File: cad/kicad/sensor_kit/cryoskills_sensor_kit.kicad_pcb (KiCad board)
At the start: 2 copper layers, 150 x 60 mm, 51 parts, among them J1 PWR_In, J10 QWIIC_I2C_2, J11 QWIIC_I2C_3, J12 DS18B20, J2 PWR_SENSE_Panel, J3 PWR_SENSE_Battery, J4 Conn_01x02, J5 Conn_01x02, J6 Conn_01x02, J7 PT1000_RTD, J8 SPI_BREAKOUT, J9 QWIIC_I2C_1, SW1 SPDT Switch, U1 LM317_TO-220, U2 RFM96W, U3 INA3221, U4 LM334Z

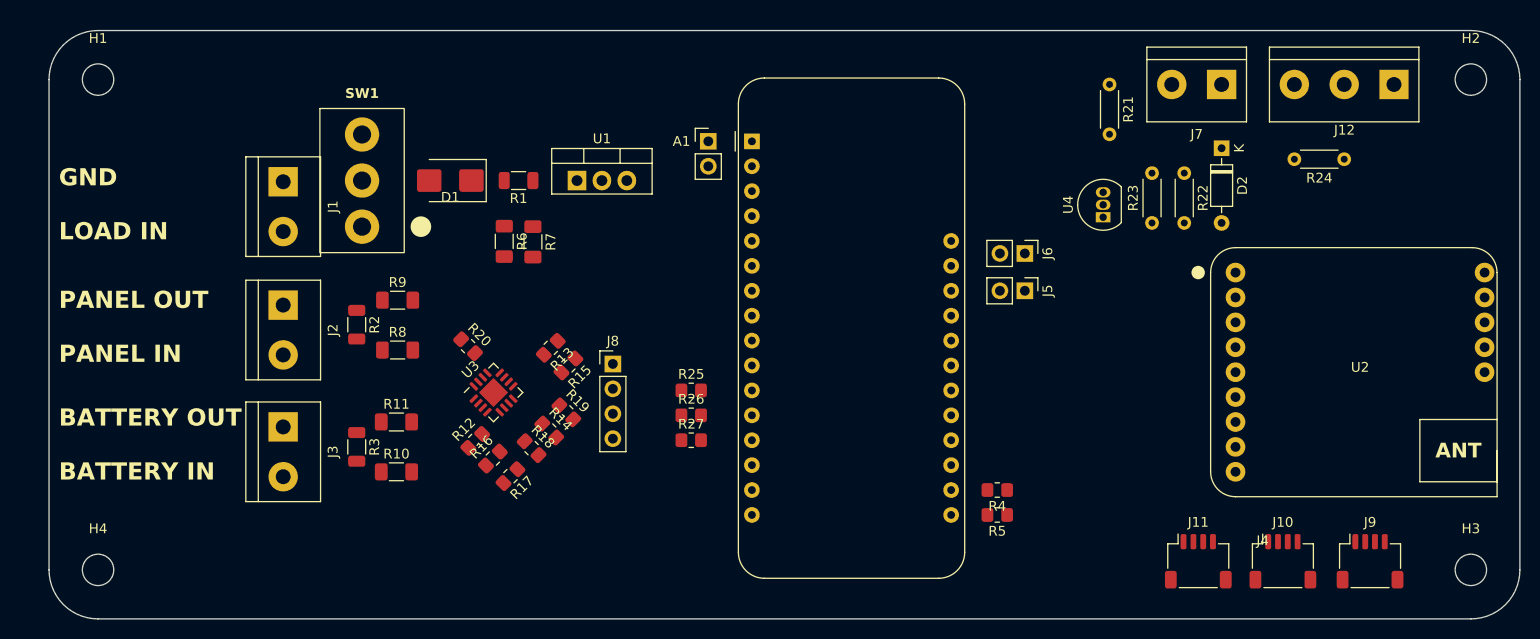
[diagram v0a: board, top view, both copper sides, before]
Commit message: updates sensorkit PCB with revised pinout and wheatstone bridge circuit
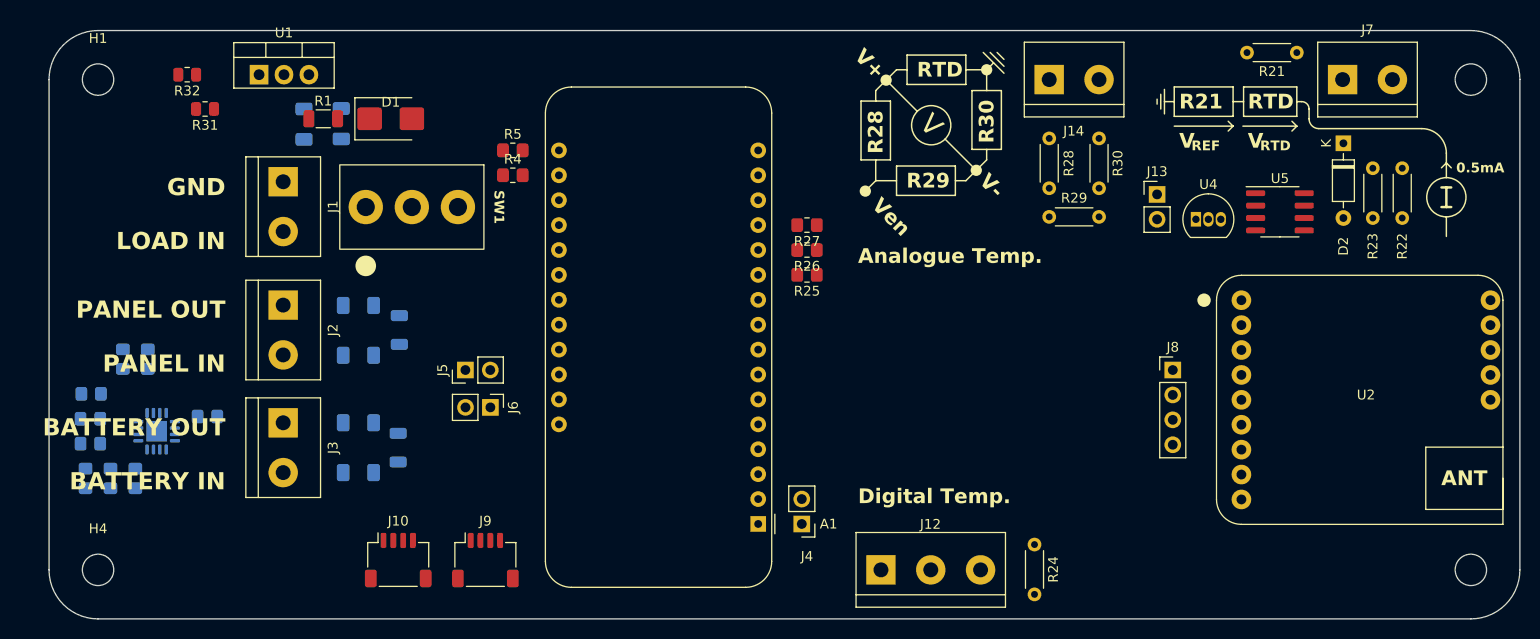
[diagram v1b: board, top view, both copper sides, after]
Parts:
- removed J11: QWIIC_I2C_3, Connector_JST:JST_SH_SM04B-SRSS-TB_1x04-1MP_P1.00mm_Horizontal
- added J13: Conn_01x02, Connector_PinHeader_2.54mm:PinHeader_1x02_P2.54mm_Vertical, F.Cu at (171.5, 88.7)
- added J14: PT1000_RTD_WHEAT, cryoskills_sensor_kit:TerminalBlock_Multicomp_5.08_2way_MP012059, F.Cu at (160.5, 77.0)
- added R28: 3k, Resistor_THT:R_Axial_DIN0204_L3.6mm_D1.6mm_P5.08mm_Horizontal, F.Cu at (160.5, 88.1)
- added R29: 3k, Resistor_THT:R_Axial_DIN0204_L3.6mm_D1.6mm_P5.08mm_Horizontal, F.Cu at (160.5, 91.0)
- added R30: 1k, Resistor_THT:R_Axial_DIN0204_L3.6mm_D1.6mm_P5.08mm_Horizontal, F.Cu at (165.6, 88.1)
- added R31: 1.2k, Resistor_SMD:R_0805_2012Metric, F.Cu at (74.4, 80.0)
- added R32: 1.8k, Resistor_SMD:R_0805_2012Metric, F.Cu at (72.6, 76.5)
- added U5: LM234Z-3, Package_SO:SOIC-8_3.9x4.9mm_P1.27mm, F.Cu at (184.0, 90.5)
- J7: value PT1000_RTD -> PT1000_RTD_CC
- R10, R11, R12, R13, R14, R15, R16, R17, R18, R19, R2, R20, R3, R6, R7, R8, R9, U3: moved to B.Cu
- moved J10 90.2 mm to (94.1, 126.0)
- moved J9 90.2 mm to (103.0, 126.0)
- moved J12 72.0 mm to (143.3, 127.0), turned to 0 degrees
- moved R5 61.8 mm to (105.8, 84.2), turned to 0 degrees
- moved R4 58.9 mm to (105.8, 86.8), turned to 0 degrees
- moved J5 57.6 mm to (101.0, 106.6), turned to 90 degrees
- moved J8 57.1 mm to (173.1, 106.6)
- moved J6 56.7 mm to (103.5, 110.4)
- moved R24 50.4 mm to (159.0, 124.4), turned to -90 degrees
- moved R19 48.5 mm to (62.8, 109.1), turned to 180 degrees
- moved R14 46.8 mm to (62.7, 111.6), turned to 180 degrees
- moved R15 45.4 mm to (66.0, 105.5), turned to -90 degrees
- moved R18 45.0 mm to (62.7, 114.1), turned to 180 degrees
- moved R17 43.3 mm to (62.2, 117.7), turned to -90 degrees
- moved R13 41.1 mm to (68.6, 105.5), turned to -90 degrees
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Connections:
- net Net-(D2-A) renamed /Sensors/CC_OUT
- net Net-(R22-Pad1) renamed /Sensors/CC_ADJ
- A1 pad 22: unconnected-(A1-D10-Pad22) -> /RADIO_IRQ
- A1 pad 23: unconnected-(A1-D11-Pad23) -> /RTD_WHEAT_EN
- U1 pad 1: GND -> Net-(U1-ADJ)
- U2 pad 4: unconnected-(U2-G0-Pad4) -> /RADIO_IRQ
- U4 pad 1: /VCC_3V3 -> /Sensors/CC_IN
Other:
- board text added: "0.5mA"
- board text added: "Analogue Temp."
- board text added: "Digital Temp."
- board text added: "R21"
- board text added: "R28"
- board text added: "R29"
- board text added: "R30"
- board text added: "REF"
- board text added: "RTD"
- board text added: "V"
- board text added: "V+"
- board text added: "V-"
- board text added: "Ven"

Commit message: makes small PCB modifications
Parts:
- moved R7 1.05 mm to (84.5, 82.6)
- moved R6 1.05 mm to (88.3, 82.5)
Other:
- board text added: "ADALOGGER"
- board text added: "BATTERY"
- board text added: "RADIO MODULE"
- board text added: "USB"
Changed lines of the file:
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@@
     (property "SupplierPartNo" "124-5502")
     (attr through_hole)
-    (fp_text reference "U2" (at 0 -0.5 unlocked) (layer "F.SilkS")
+    (fp_text reference "U2" (at -9.3 11.34 unlocked) (layer "F.SilkS")
         (effects (font (size 1 1) (thickness 0.1)))
     )
@@
   )
   (footprint "Resistor_SMD:R_1206_3216Metric_Pad1.30x1.75mm_HandSolder" (layer "B.Cu")
-    (at 88.3 81.5 90)
+    (at 88.3 82.55 90)
     (descr "Resistor SMD 1206 (3216 Metric), square (rectangular) end terminal, IPC_7351 nominal with elongated pad for handsoldering. (Body size source: IPC-SM-782 page 72, https://www.pcb-3d.com/wordpress/wp-content/uploads/ipc-sm-782a_amendment_1_and_2.pdf), generated with kicad-footprint-generator")
     (tags "resistor handsolder")
@@
   )
   (footprint "Resistor_SMD:R_1206_3216Metric_Pad1.30x1.75mm_HandSolder" (layer "B.Cu")
-    (at 84.5 81.550001 90)
+    (at 84.5 82.600001 90)
     (descr "Resistor SMD 1206 (3216 Metric), square (rectangular) end terminal, IPC_7351 nominal with elongated pad for handsoldering. (Body size source: IPC-SM-782 page 72, https://www.pcb-3d.com/wordpress/wp-content/uploads/ipc-sm-782a_amendment_1_and_2.pdf), generated with kicad-footprint-generator")
     (tags "resistor handsolder")
@@
   (gr_line (start 154.12132 78.121321) (end 154.12132 76)
     (stroke (width 0.15) (type default)) (layer "F.SilkS"))
+  (gr_line (start 100.5 96.8) (end 100.5 95.2)
+    (stroke (width 0.5) (type default)) (layer "F.SilkS"))
   (gr_line (start 186.25 79.25) (end 185.75 79.25)
     (stroke (width 0.15) (type default)) (layer "F.SilkS"))
@@
     (effects (font (size 1 1) (thickness 0.2) bold) (justify left))
   )
+  (gr_text "ADALOGGER" (at 121.633175 104.135676 45) (layer "F.SilkS")
+    (effects (font (size 1.75 1.75) (thickness 0.4) bold) (justify bottom))
+  )
   (gr_text "V" (at 180.75 83.25) (layer "F.SilkS")
     (effects (font (size 1.5 1.5) (thickness 0.3) bold) (justify left))
@@
     (effects (font (size 1.75 1.75) (thickness 0.4) bold) (justify right bottom))
   )
+  (gr_text "RADIO\nMODULE" (at 193.379312 111.521812 45) (layer "F.SilkS")
+    (effects (font (size 1.75 1.75) (thickness 0.4) bold) (justify bottom))
+  )
+  (gr_text "USB" (at 101.42425 98 90) (layer "F.SilkS")
+    (effects (font (size 1.75 1.75) (thickness 0.4) bold) (justify right bottom))
+  )
   (gr_text "V" (at 173.75 83.25) (layer "F.SilkS")
     (effects (font (size 1.5 1.5) (thickness 0.3) bold) (justify left))
@@
     (effects (font (size 1.5 1.5) (thickness 0.3) bold) (justify left))
   )
+  (gr_text "BATTERY" (at 92.02425 98 90) (layer "F.SilkS")
+    (effects (font (size 1.75 1.75) (thickness 0.4) bold) (justify right bottom))
+  )
   (gr_text "R28" (at 142.807612 84.571067 90) (layer "F.SilkS")
